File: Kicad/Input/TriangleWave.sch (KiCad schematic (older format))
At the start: 6 parts

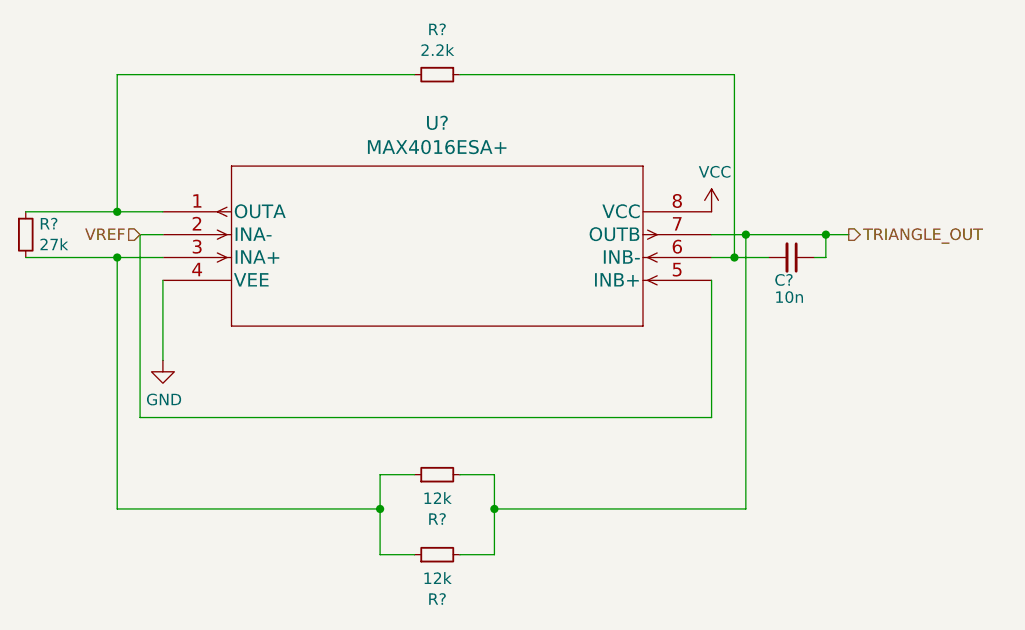
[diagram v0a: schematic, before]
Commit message: Input PCB added
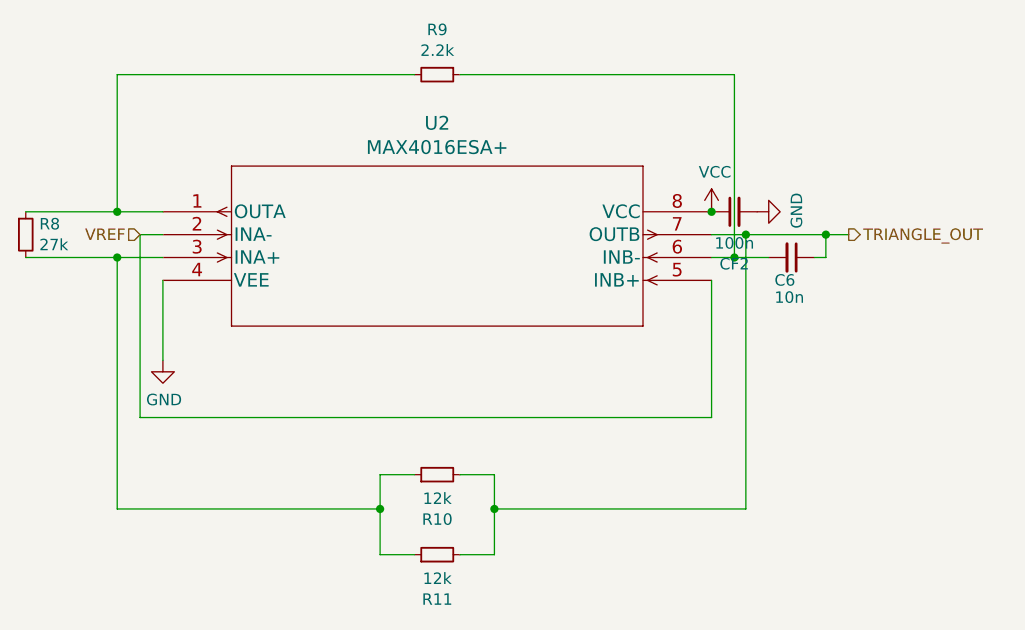
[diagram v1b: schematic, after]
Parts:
- added CF2: 100n, Capacitor_SMD:C_0603_1608Metric_Pad1.08x0.95mm_HandSolder, symbol Device:C_Small
- C6: renamed from C?; footprint Capacitor_SMD:C_0201_0603Metric_Pad0.64x0.40mm_HandSolder -> Capacitor_SMD:C_0603_1608Metric_Pad1.08x0.95mm_HandSolder
- gave numbers to parts that had none: 5
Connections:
- net GND: now also CF2.2
- net VCC: now also CF2.1
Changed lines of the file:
@@
 $Descr A4 11693 8268
 encoding utf-8
-Sheet 4 4
+Sheet 3 4
 Title ""
 Date ""
@@
 $EndDescr
 $Comp
-L power:VCC #PWR?
+L power:VCC #PWR0110
 U 1 1 610A2484
 P 6500 3450
-F 0 "#PWR?" H 6500 3300 50  0001 C CNN
+F 0 "#PWR0110" H 6500 3300 50  0001 C CNN
 F 1 "VCC" H 6515 3623 50  0000 C CNN
 F 2 "" H 6500 3450 50  0001 C CNN
@@
 $EndComp
 $Comp
-L power:GND #PWR?
+L power:GND #PWR0111
 U 1 1 610A5C03
 P 4100 4100
-F 0 "#PWR?" H 4100 3850 50  0001 C CNN
+F 0 "#PWR0111" H 4100 3850 50  0001 C CNN
 F 1 "GND" H 4105 3927 50  0000 C CNN
 F 2 "" H 4100 4100 50  0001 C CNN
@@
 TRIANGLE_OUT
 $Comp
-L Device:R_Small R?
+L Device:R_Small R9
 U 1 1 610ABFC7
 P 5300 2850
-F 0 "R?" V 5104 2850 50  0000 C CNN
+F 0 "R9" V 5104 2850 50  0000 C CNN
 F 1 "2.2k" V 5195 2850 50  0000 C CNN
 F 2 "Resistor_SMD:R_0603_1608Metric_Pad0.98x0.95mm_HandSolder" H 5300 2850 50  0001 C CNN
@@
 	4100 4100 4100 3750
 $Comp
-L Device:C_Small C?
+L Device:C_Small C6
 U 1 1 610B0597
 P 6850 3650
-F 0 "C?" V 6950 3575 50  0000 L CNN
+F 0 "C6" V 6950 3575 50  0000 L CNN
 F 1 "10n" V 7025 3575 50  0000 L CNN
-F 2 "Capacitor_SMD:C_0201_0603Metric_Pad0.64x0.40mm_HandSolder" H 6850 3650 50  0001 C CNN
+F 2 "Capacitor_SMD:C_0603_1608Metric_Pad1.08x0.95mm_HandSolder" H 6850 3650 50  0001 C CNN
 F 3 "~" H 6850 3650 50  0001 C CNN
 	1    6850 3650
@@
 	7000 3550 7100 3550
 $Comp
-L Device:R_Small R?
+L Device:R_Small R10
 U 1 1 610B770E
 P 5300 4600
-F 0 "R?" V 5104 4600 50  0000 C CNN
+F 0 "R10" V 5104 4600 50  0000 C CNN
 F 1 "12k" V 5195 4600 50  0000 C CNN
 F 2 "Resistor_SMD:R_0603_1608Metric_Pad0.98x0.95mm_HandSolder" H 5300 4600 50  0001 C CNN
@@
 	3900 3450 3500 3450
 $Comp
-L Device:R_Small R?
+L Device:R_Small R8
 U 1 1 610B9D20
 P 3500 3550
-F 0 "R?" H 3559 3596 50  0000 L CNN
+F 0 "R8" H 3559 3596 50  0000 L CNN
 F 1 "27k" H 3559 3505 50  0000 L CNN
 F 2 "Resistor_SMD:R_0603_1608Metric_Pad0.98x0.95mm_HandSolder" H 3500 3550 50  0001 C CNN
@@
 	6950 3650 7000 3650
 Wire Wire Line
-	6500 3650 6600 3650
-Wire Wire Line
 	6500 3550 6650 3550
 Connection ~ 6650 3550
@@
 Wire Wire Line
 	6600 3650 6600 2850
-Connection ~ 6600 3650
-Wire Wire Line
-	6600 3650 6750 3650
-$Comp
-L Device:R_Small R?
+$Comp
+L Device:R_Small R11
 U 1 1 6110AB92
 P 5300 4950
-F 0 "R?" V 5104 4950 50  0000 C CNN
+F 0 "R11" V 5104 4950 50  0000 C CNN
 F 1 "12k" V 5195 4950 50  0000 C CNN
 F 2 "Resistor_SMD:R_0603_1608Metric_Pad0.98x0.95mm_HandSolder" H 5300 4950 50  0001 C CNN
@@
 	5050 4750 5050 4950
 $Comp
-L MAX4016ESA:MAX4016ESA+ U?
+L MAX4016ESA:MAX4016ESA+ U2
 U 1 1 610FB9E0
 P 4100 3450
-F 0 "U?" H 5300 3837 60  0000 C CNN
+F 0 "U2" H 5300 3837 60  0000 C CNN
 F 1 "MAX4016ESA+" H 5300 3731 60  0000 C CNN
 F 2 "MAX4016ESA:MAX4016ESA&plus_" H 5300 3690 60  0001 C CNN
@@
 	1    0    0    -1
 $EndComp
+$Comp
+L Device:C_Small CF?
+U 1 1 6116AC18
+P 6600 3450
+AR Path="/610C616D/6116AC18" Ref="CF?"  Part="1"
+AR Path="/611D4178/6116AC18" Ref="CF?"  Part="1"
+AR Path="/6113023B/6116AC18" Ref="CF?"  Part="1"
+AR Path="/611302FE/6116AC18" Ref="CF2"  Part="1"
+F 0 "CF2" V 6371 3450 50  0000 C CNN
+F 1 "100n" V 6462 3450 50  0000 C CNN
+F 2 "Capacitor_SMD:C_0603_1608Metric_Pad1.08x0.95mm_HandSolder" H 6600 3450 50  0001 C CNN
+F 3 "~" H 6600 3450 50  0001 C CNN
+	1    6600 3450
+	0    -1   -1   0
+$EndComp
+$Comp
+L power:GND #PWR?
+U 1 1 6116AC1E
+P 6700 3450
+AR Path="/6113023B/6116AC1E" Ref="#PWR?"  Part="1"
+AR Path="/611302FE/6116AC1E" Ref="#PWR0120"  Part="1"
+F 0 "#PWR0120" H 6700 3200 50  0001 C CNN
+F 1 "GND" H 6705 3277 50  0000 C CNN
+F 2 "" H 6700 3450 50  0001 C CNN
+F 3 "" H 6700 3450 50  0001 C CNN
+	1    6700 3450
+	0    -1   -1   0
+$EndComp
+Wire Wire Line
+	6500 3650 6600 3650
+Connection ~ 6600 3650
+Wire Wire Line
+	6600 3650 6750 3650
+Connection ~ 6500 3450
 $EndSCHEMATC
